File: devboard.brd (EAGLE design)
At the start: 31.5 x 55 mm, 40 parts, among them IC1 ATMEGA1284, Q1 CRYSTALX22, X1 MICROMATCH-8

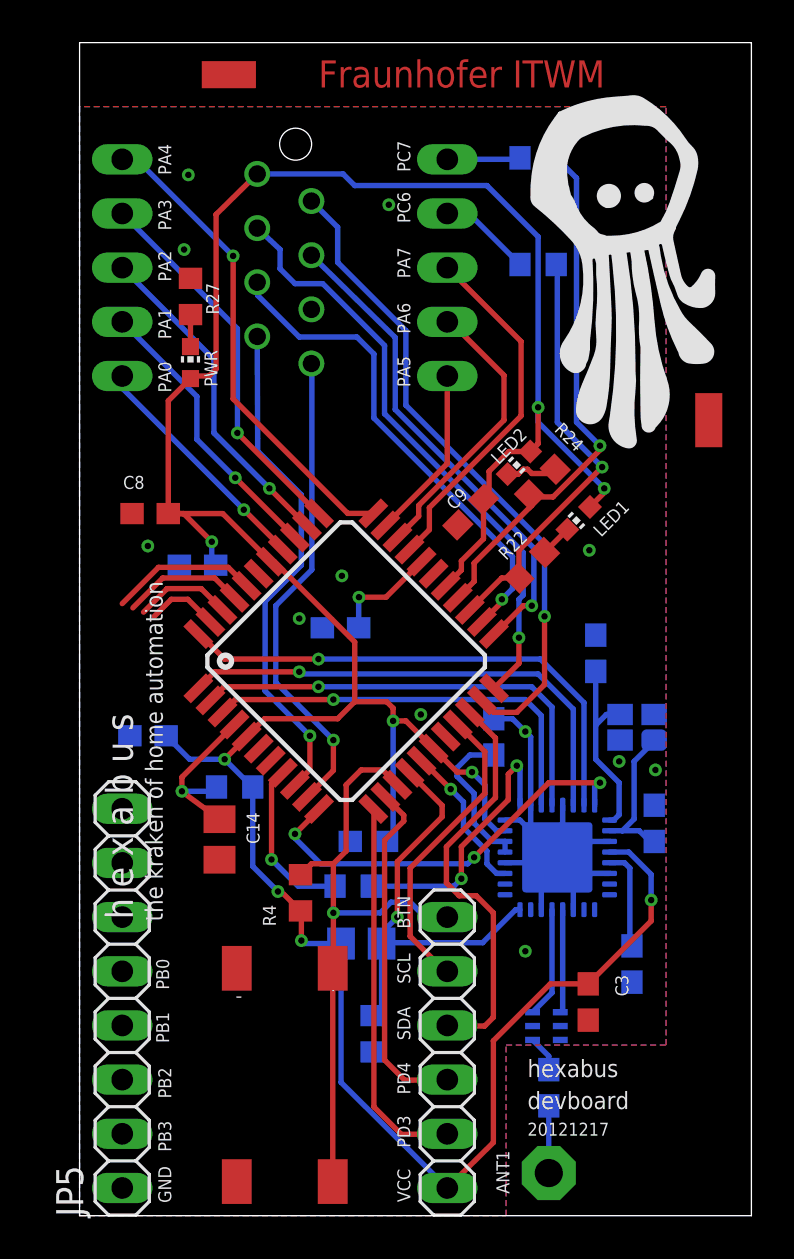
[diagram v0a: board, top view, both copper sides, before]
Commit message: updated to include MISO,MOSI,SCLK to external pins
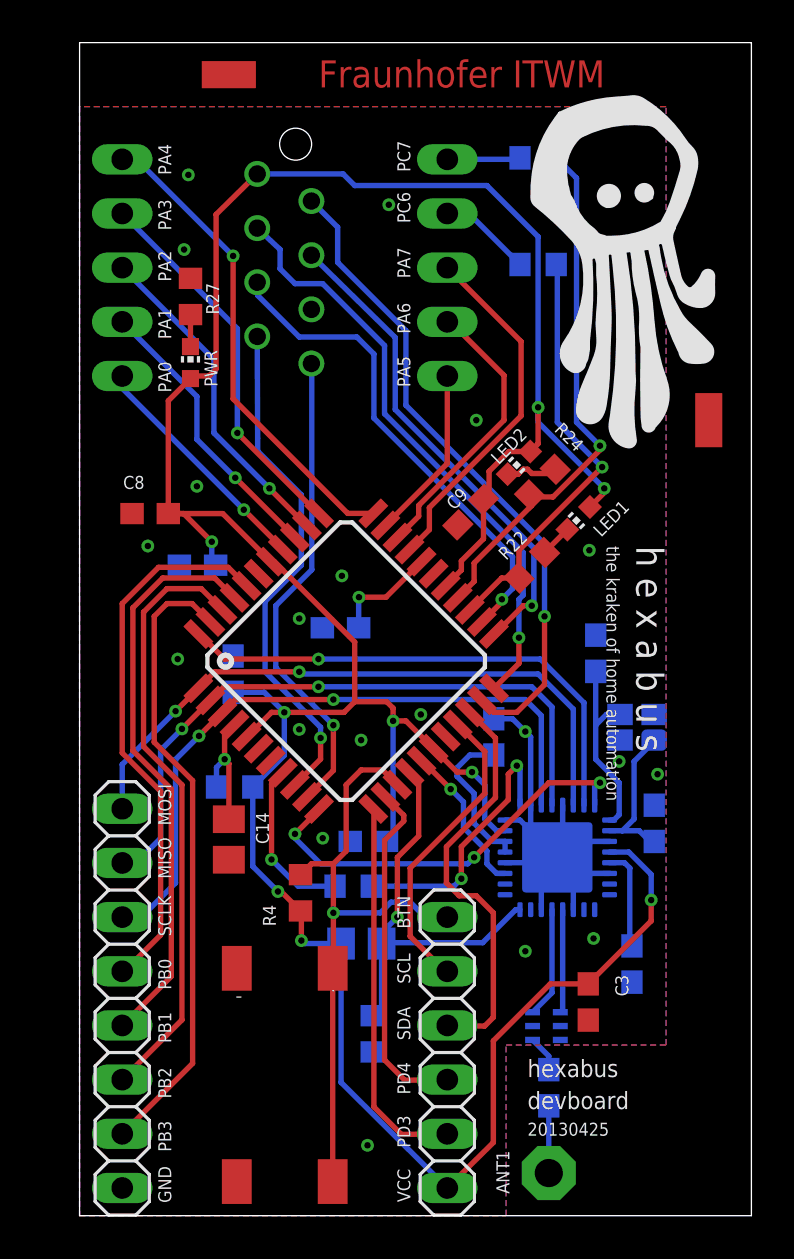
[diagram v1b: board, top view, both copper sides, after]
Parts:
- moved C26 4.93 mm to (7.20, 25.4), turned to 90 degrees
- moved C14 0.44 mm to (7.00, 17.6)
- renumbered JP5 to JP4
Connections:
- removed net N$18: JP4.6
- removed net N$19: JP4.7
- removed net N$20: JP4.8
- net MISO: now also JP4.7
- net MOSI: now also JP4.8
- net SCLK: now also JP4.6
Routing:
- net PB3: track 3.41 -> 29.6 mm
- net PB2: track 4.57 -> 28.4 mm
- net PB1: track 5.73 -> 27.0 mm
- net PB0: track 6.90 -> 25.7 mm
- net SCLK: track 19.7 -> 31.8 mm, vias 1 -> 2
- net MISO: track 21.3 -> 31.0 mm, vias 1 -> 2
- net MOSI: track 23.1 -> 30.3 mm, vias 1 -> 2
- net N$11: track 8.07 -> 6.17 mm
- net AT_RST: track 20.6 -> 19.6 mm
- net GND: vias 12 -> 20
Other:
- board text added: "20130425"
- board text added: "MISO"
- board text added: "MOSI"
- board text added: "SCLK"
- board text removed: "20121217"

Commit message: changed C13, C14 to 0603
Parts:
- C13, C14: device rcl:C0805 -> rcl:C0603
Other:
- board text added: "20130725"
- board text removed: "20130425"
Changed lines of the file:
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@@
 <text x="21" y="6.5" size="0.8128" layer="21" font="vector" ratio="12">hexabus</text>
 <text x="21" y="5" size="0.8128" layer="21" font="vector">devboard</text>
-<text x="21" y="3.75" size="0.6096" layer="21" font="vector">20130425</text>
+<text x="21" y="3.75" size="0.6096" layer="21" font="vector">20130725</text>
 <text x="14.9" y="15" size="0.6096" layer="21" font="vector" rot="R270">BTN</text>
 <hole x="10.13" y="50.24" drill="1.5"/>
@@
 </autorouter>
 <elements>
-<element name="C13" library="rcl" package="C0805" value="220nF" x="13.21" y="12.76" smashed="yes" rot="MR180">
+<element name="C13" library="rcl" package="C0603" value="220nF" x="13.21" y="12.76" smashed="yes" rot="MR180">
 <attribute name="NAME" x="11.94" y="11.49" size="0.6096" layer="26" rot="MR180"/>
 </element>
@@
 <attribute name="NAME" x="25.12" y="11.29" size="0.6096" layer="25" rot="R270"/>
 </element>
-<element name="C14" library="rcl" package="C0805" value="100nF" x="7" y="17.64" smashed="yes" rot="R270">
+<element name="C14" library="rcl" package="C0603" value="100nF" x="7" y="17.64" smashed="yes" rot="R270">
 <attribute name="NAME" x="8.27" y="18.91" size="0.6096" layer="25" rot="R270"/>
 </element>
@@
 <wire x1="7.267409375" y1="23.03015" x2="6.8" y2="22.562740625" width="0.254" layer="1"/>
 <wire x1="6.8" y1="22.562740625" x2="6.8" y2="21.4" width="0.254" layer="1"/>
-<wire x1="7" y1="18.59" x2="7" y2="21.2" width="0.254" layer="1"/>
+<wire x1="7" y1="18.49" x2="7" y2="21.2" width="0.254" layer="1"/>
 <wire x1="7" y1="21.2" x2="6.8" y2="21.4" width="0.254" layer="1"/>
 </signal>
@@
 <contactref element="R3" pad="2"/>
 <wire x1="13.72" y1="9.38" x2="14.16" y2="9.74" width="0.254" layer="16"/>
-<wire x1="14.16" y1="9.74" x2="14.16" y2="12.76" width="0.254" layer="16"/>
+<wire x1="14.16" y1="9.74" x2="14.06" y2="12.76" width="0.254" layer="16"/>
 <wire x1="20.45" y1="14.35" x2="20.65" y2="14.35" width="0.254" layer="16"/>
 <wire x1="18.9" y1="12.8" x2="20.45" y2="14.35" width="0.254" layer="16"/>
 <wire x1="14.2" y1="12.8" x2="18.9" y2="12.8" width="0.254" layer="16"/>
-<wire x1="14.16" y1="12.76" x2="14.2" y2="12.8" width="0.254" layer="16"/>
-<wire x1="14.16" y1="12.76" x2="14.16" y2="13.26" width="0.254" layer="16"/>
+<wire x1="14.06" y1="12.76" x2="14.2" y2="12.8" width="0.254" layer="16"/>
+<wire x1="14.06" y1="12.76" x2="14.16" y2="13.26" width="0.254" layer="16"/>
 <wire x1="14.16" y1="13.26" x2="14.9" y2="14" width="0.254" layer="16"/>
 <via x="14.9" y="14" extent="1-16" drill="0.3"/>
@@
 <wire x1="9.45" y1="15.2" x2="9.3" y2="15.2" width="0.254" layer="1"/>
 <wire x1="10.36" y1="14.29" x2="9.45" y2="15.2" width="0.254" layer="1"/>
-<wire x1="12.26" y1="12.76" x2="10.54" y2="12.76" width="0.254" layer="16"/>
+<wire x1="12.36" y1="12.76" x2="10.54" y2="12.76" width="0.254" layer="16"/>
 <wire x1="10.54" y1="12.76" x2="10.4" y2="12.9" width="0.254" layer="16"/>
 <wire x1="10.4" y1="12.9" x2="10.4" y2="14.25" width="0.254" layer="1"/>
@@
 <wire x1="14.3999" y1="24.1" x2="14.7" y2="23.7999" width="0.254" layer="1"/>
 <wire x1="17.24" y1="1.3" x2="12.26" y2="6.25" width="0.254" layer="16"/>
-<wire x1="12.26" y1="6.25" x2="12.26" y2="12.76" width="0.254" layer="16"/>
+<wire x1="12.26" y1="6.25" x2="12.36" y2="12.76" width="0.254" layer="16"/>
 <wire x1="4.16" y1="32.92" x2="4.16" y2="38.21" width="0.254" layer="1"/>
 <wire x1="4.16" y1="38.21" x2="5.2" y2="39.25" width="0.254" layer="1"/>

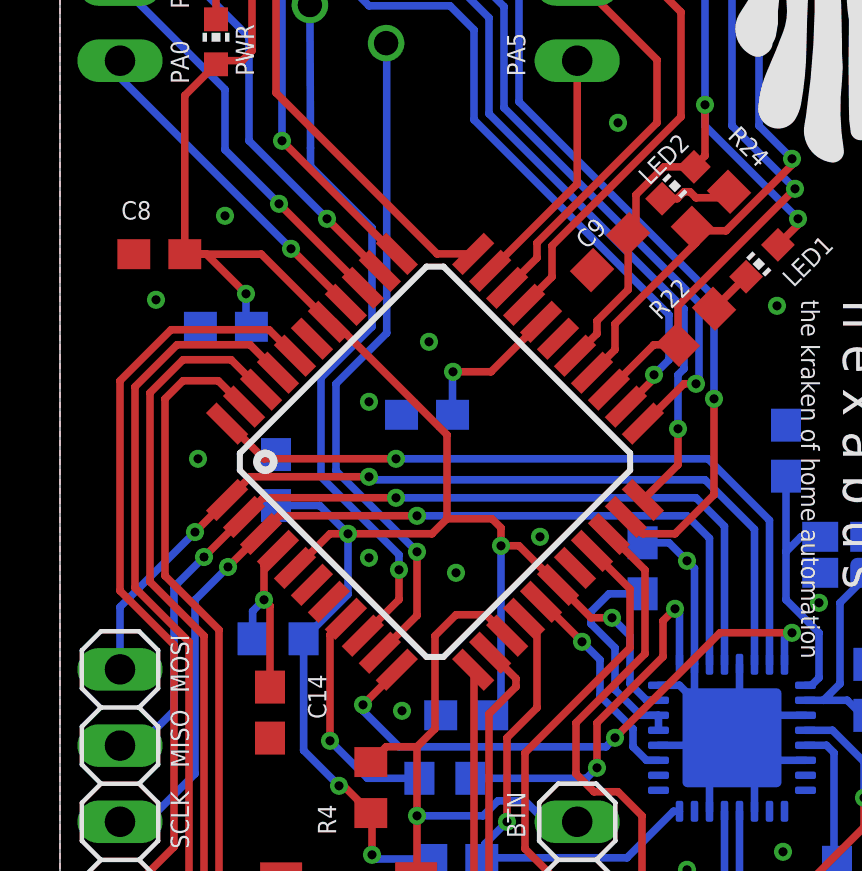
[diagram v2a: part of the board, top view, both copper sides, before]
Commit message: changed atmega to nonambiguous package
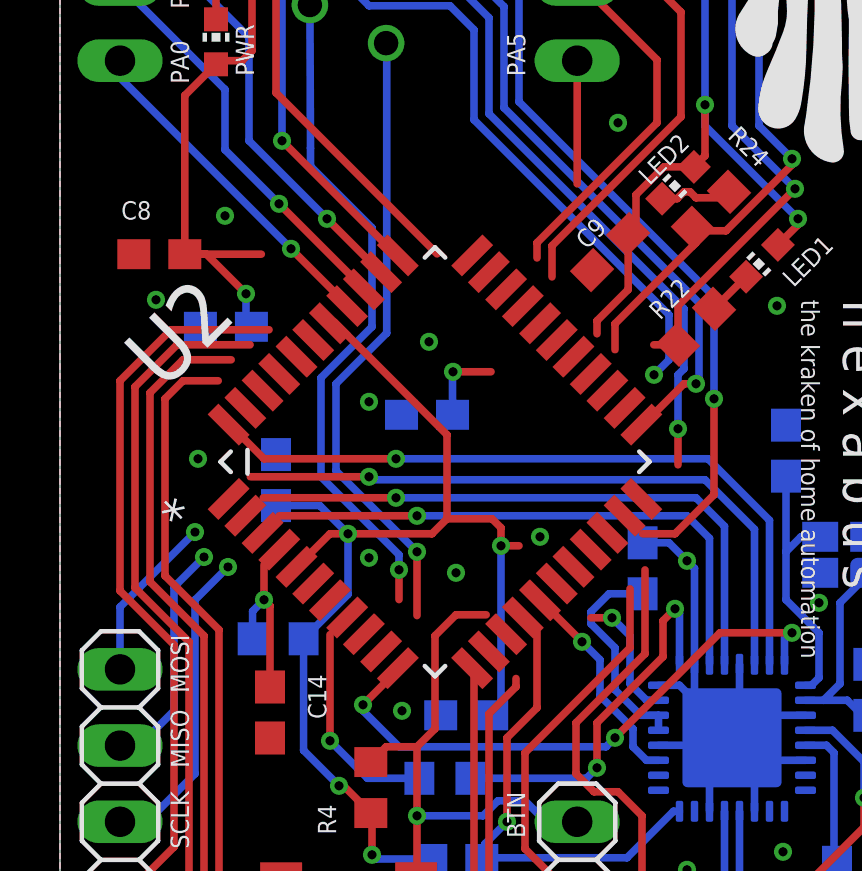
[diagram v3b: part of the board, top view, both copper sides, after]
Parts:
- removed IC1: ATMEGA1284, atmel:TQFP44
- added U2: ATMEGA1284-AU, hexabus:QFP80P1200X1200X120-44N
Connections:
- removed net N$10: C19.1, IC1.29
- removed net N$11: C14.1, IC1.4, R10.1
- removed net N$12: IC1.7
- removed net N$3: U1.9
- removed net N$6: U1.10
- removed net N$7: U1.1
- removed net N$8: U1.2
- new net !RESET: C14.1, R10.1, U2.4
- new net AREF: C19.1, U2.29
- net AT_RST: now also U2.15; no longer IC1.15
- net BTN: now also U2.14; no longer IC1.14
- net CLKM: now also U2.8; no longer IC1.8
- net GND: now also U2.18, U2.28, U2.39, U2.6; no longer IC1.18, IC1.28, IC1.39, IC1.6
- net IRQ: now also U2.11; no longer IC1.11
- net LED1: now also U2.25; no longer IC1.25
- net LED2: now also U2.26; no longer IC1.26
- net MISO: now also U2.2; no longer IC1.2
- net MOSI: now also U2.1; no longer IC1.1
- net PA0: now also U2.37; no longer IC1.37
- net PA1: now also U2.36; no longer IC1.36
- net PA2: now also U2.35; no longer IC1.35
- net PA3: now also U2.34; no longer IC1.34
- net PA4: now also U2.33; no longer IC1.33
- net PA5: now also U2.32; no longer IC1.32
- net PA6: now also U2.31; no longer IC1.31
- net PA7: now also U2.30; no longer IC1.30
- net PB0: now also U2.40; no longer IC1.40
- net PB1: now also U2.41; no longer IC1.41
- net PB2: now also U2.42; no longer IC1.42
- net PB3: now also U2.43; no longer IC1.43
- net PD3: now also U2.12; no longer IC1.12
- net PD4: now also U2.13; no longer IC1.13
- net RXD: now also U2.9; no longer IC1.9
- net SCL: now also U2.19; no longer IC1.19
- net SCLK: now also U2.3; no longer IC1.3
- net SDA: now also U2.20; no longer IC1.20
- net SEL1: now also U2.44; no longer IC1.44
- net SLP_TR: now also U2.16; no longer IC1.16
- net TCK: now also U2.21; no longer IC1.21
- net TDI: now also U2.24; no longer IC1.24
- net TDO: now also U2.23; no longer IC1.23
- net TMS: now also U2.22; no longer IC1.22
- net TXD: now also U2.10; no longer IC1.10
- net VCC: now also U2.17, U2.27, U2.38, U2.5; no longer IC1.17, IC1.27, IC1.38, IC1.5
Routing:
- net VCC: track 151.1 -> 143.3 mm
- net N$11: track 6.27 -> 0.00 mm, vias 1 -> 0
- net !RESET: track 0.00 -> 5.61 mm, vias 0 -> 1
- net N$10: track 5.07 -> 0.00 mm, vias 1 -> 0
- net PA5: track 8.21 -> 4.10 mm
- net MISO: track 31.0 -> 28.2 mm
- net AREF: track 0.00 -> 2.71 mm, vias 0 -> 1
- net MOSI: track 30.3 -> 27.6 mm
- net SCLK: track 31.8 -> 29.4 mm
- net LED1: track 20.1 -> 18.0 mm
- net SCL: track 14.3 -> 12.5 mm
- net TXD: track 22.7 -> 20.9 mm
- net RXD: track 24.2 -> 22.4 mm
- net SDA: track 19.5 -> 17.8 mm
- net TMS: track 28.2 -> 26.6 mm
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
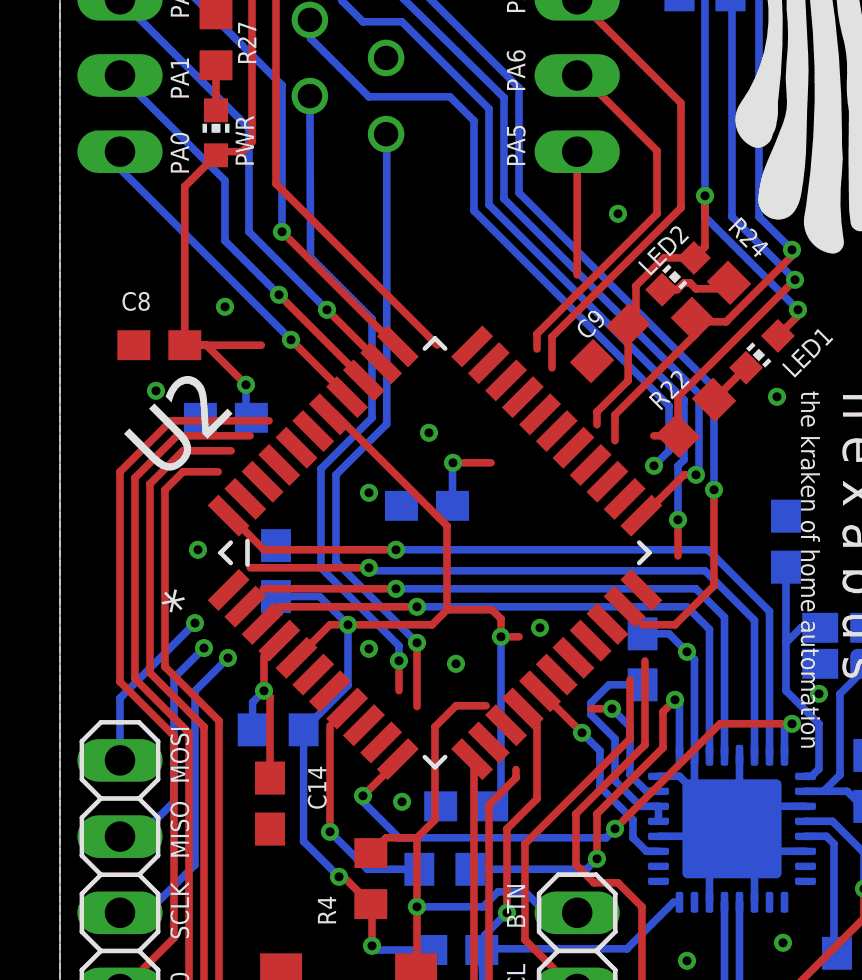
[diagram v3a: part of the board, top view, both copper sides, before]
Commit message: redrawn some wires that were lost due to swapping the atmega
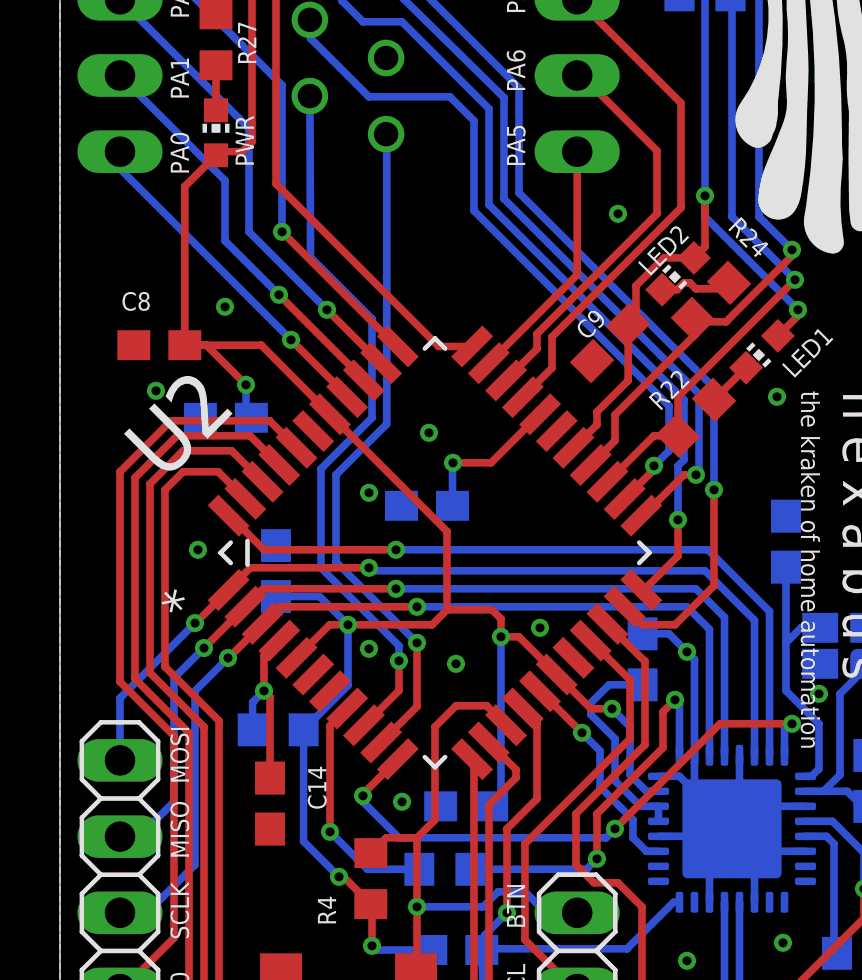
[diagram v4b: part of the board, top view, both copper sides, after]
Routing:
- net VCC: track 143.3 -> 151.0 mm
- net PA5: track 4.10 -> 8.27 mm
- net MISO: track 28.2 -> 31.0 mm
- net MOSI: track 27.6 -> 30.3 mm
- net SCLK: track 29.4 -> 31.8 mm
- net AREF: track 2.71 -> 5.01 mm
- net LED1: track 18.0 -> 20.2 mm
- net SCL: track 12.5 -> 14.4 mm
- net SDA: track 17.8 -> 19.5 mm
- net TMS: track 26.6 -> 28.3 mm
- net TXD: track 20.9 -> 22.6 mm
- net RXD: track 22.4 -> 24.1 mm
- net TDI: track 21.7 -> 23.2 mm
- net PB2: track 27.0 -> 28.5 mm
- net PA6: track 12.0 -> 13.4 mm
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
